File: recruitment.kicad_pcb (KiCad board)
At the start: 2 copper layers, 1 part

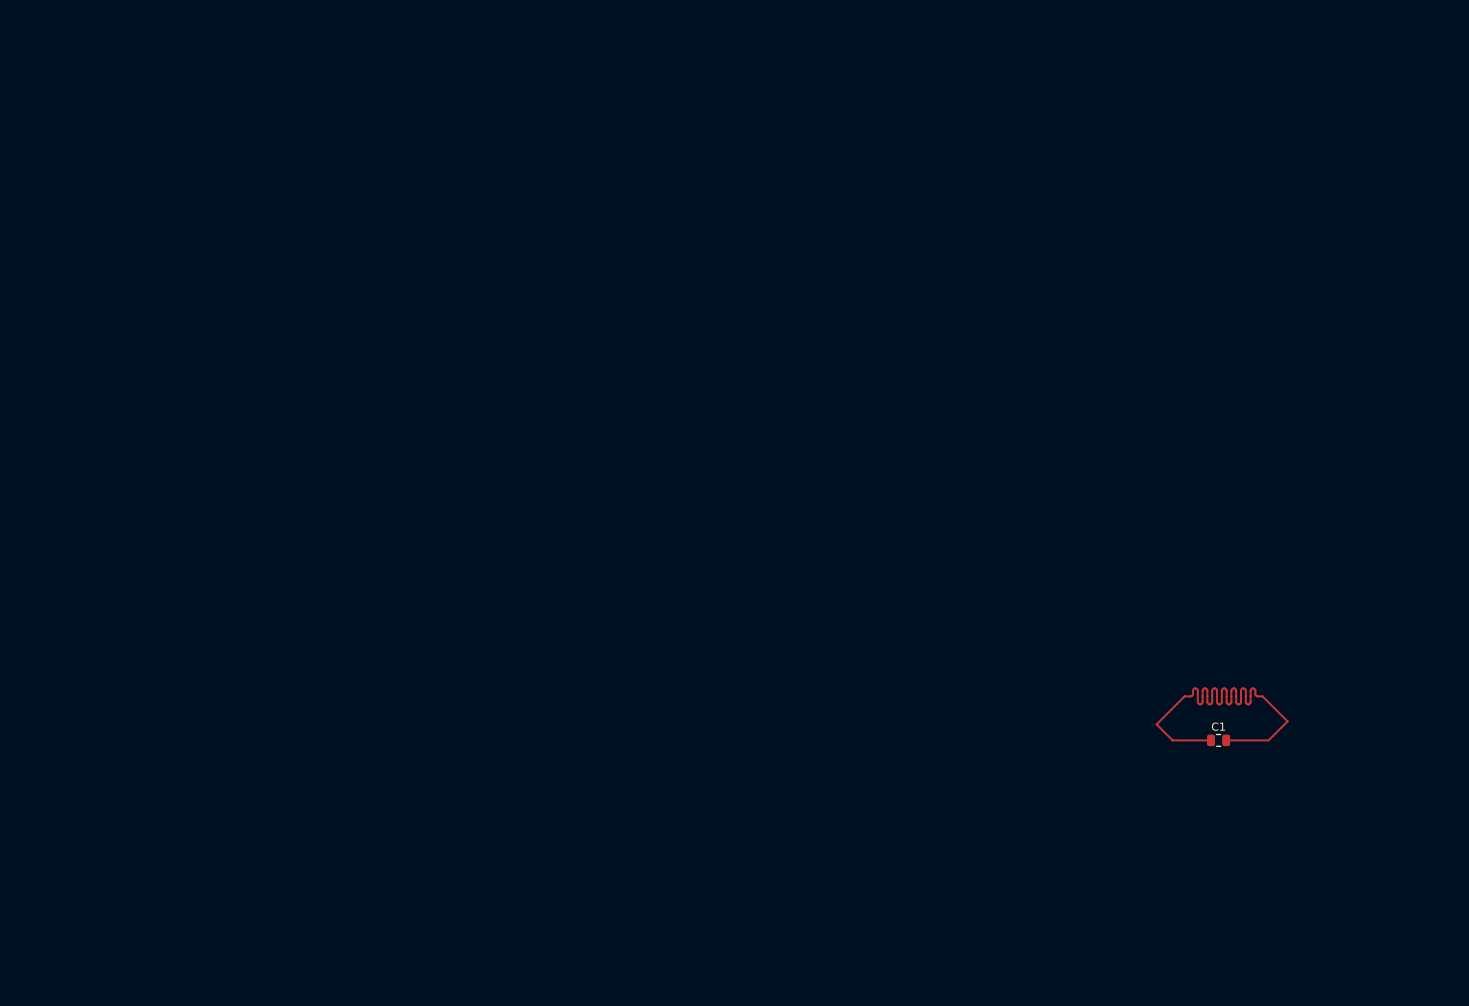
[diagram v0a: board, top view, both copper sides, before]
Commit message: feat: added hall sensor to the monitor system
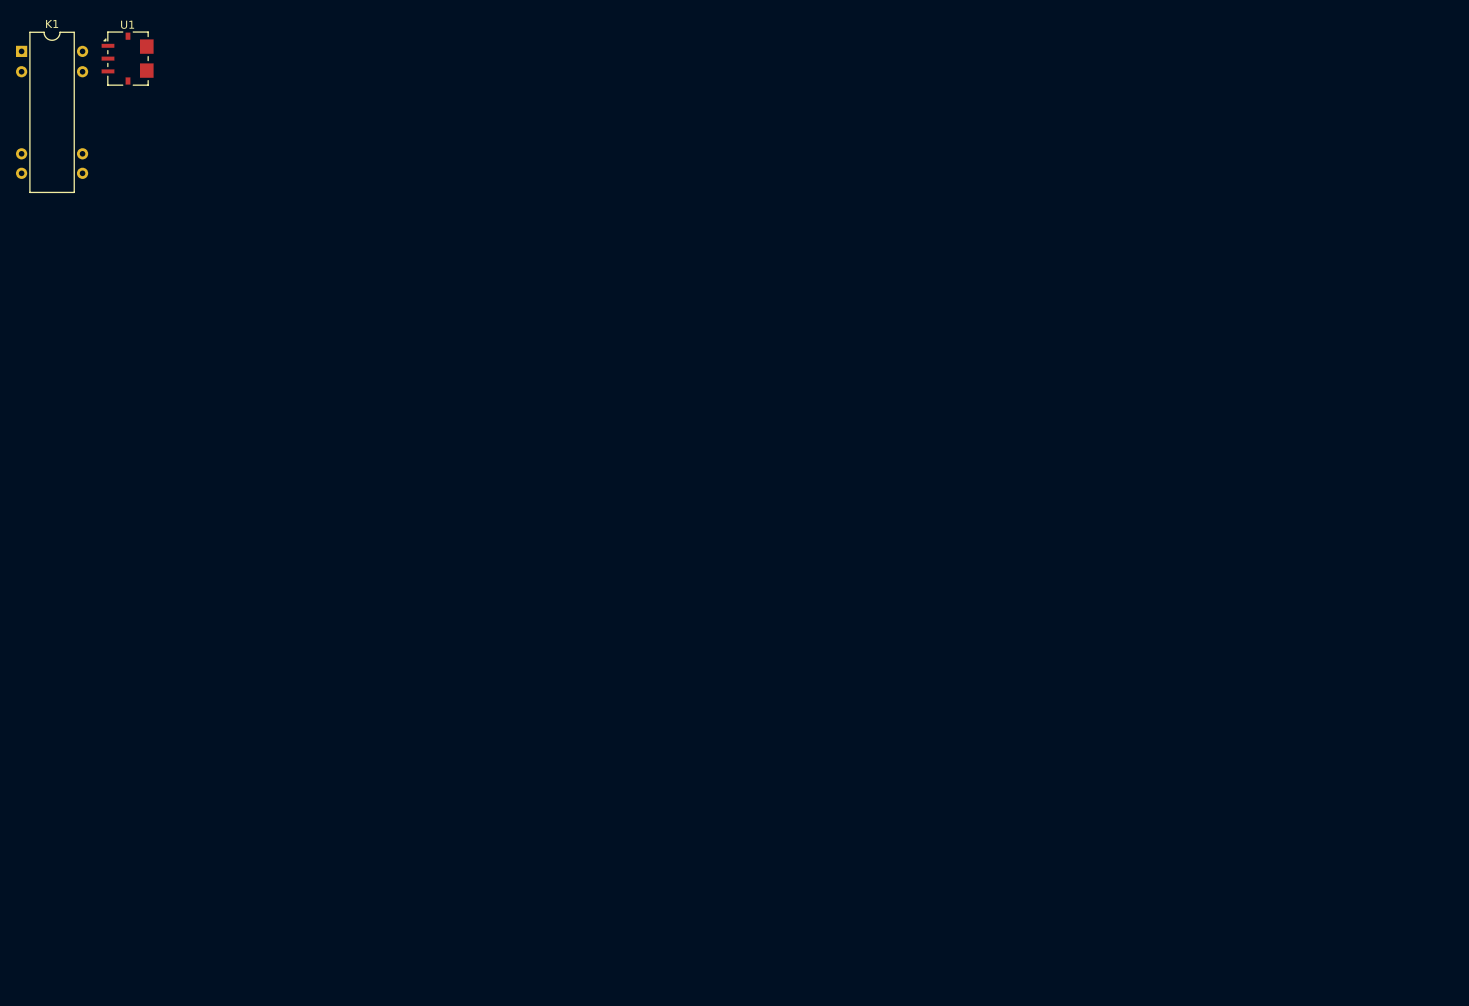
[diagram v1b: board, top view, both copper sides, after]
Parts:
- removed C1: 1F, Capacitor_SMD:C_0805_2012Metric
- added K1: DIPxx-1Axx-11x, Relay_THT:Relay_StandexMeder_DIP_LowProfile, F.Cu at (1.12, 2.62)
- added U1: ACS781xLRTR-050B, Sensor_Current:Allegro_PSOF-7_4.8x6.4mm_P1.60mm, F.Cu at (14.4, 3.52)
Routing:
- net Net-(C1-Pad1): track 57.5 -> 0.00 mm

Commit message: feat + fix on kicad pcb
feat:added mass layer

refactor: moved components for better connection

fix:added missing footprints to resistors etc.

ERC: passed warnings(3)
DRC: errors(42) ;(
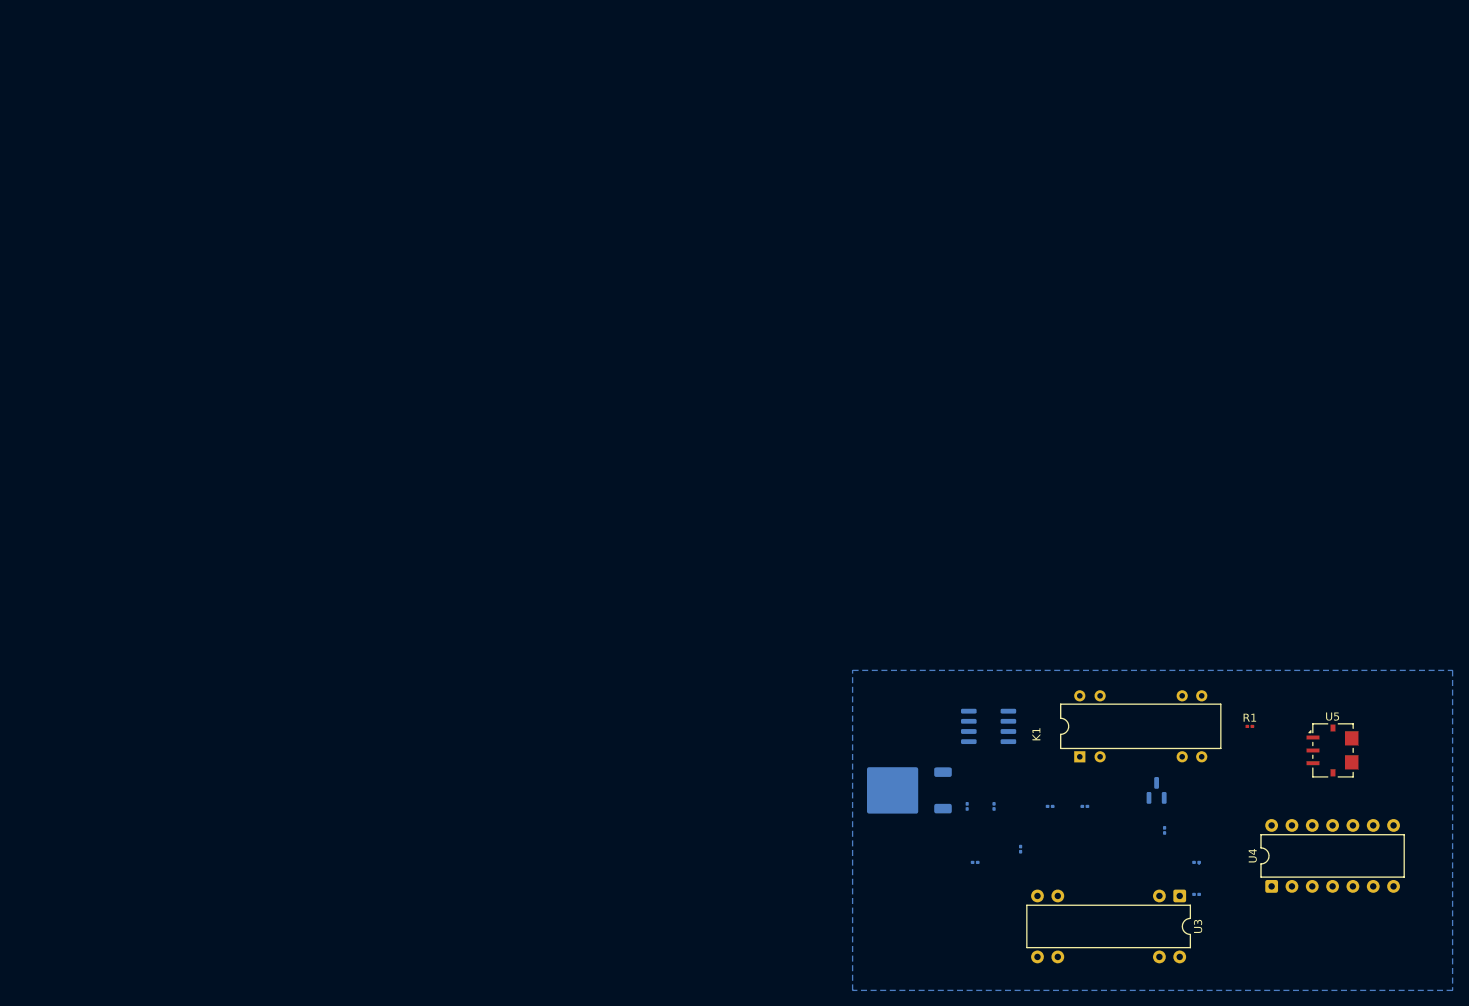
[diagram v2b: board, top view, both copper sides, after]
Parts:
- added C1: 10nF, Capacitor_SMD:C_0201_0603Metric, B.Cu at (119.3, 97.0)
- added C2: 10uF, Capacitor_SMD:C_0201_0603Metric, B.Cu at (122.7, 97.0)
- added Q1: 2N7002, Package_TO_SOT_SMD:SOT-23, B.Cu at (143.0, 95.0)
- added R1: 3,5, Resistor_SMD:R_0201_0603Metric, F.Cu at (154.7, 87.0)
- added R2: 10k, Resistor_SMD:R_0201_0603Metric, B.Cu at (126.0, 102.3)
- added R3: 1, Resistor_SMD:R_0201_0603Metric, B.Cu at (148.0, 108.0)
- added R4: 1,94, Resistor_SMD:R_0201_0603Metric, B.Cu at (129.7, 97.0)
- added R5: 1, Resistor_SMD:R_0201_0603Metric, B.Cu at (134.0, 97.0)
- added R6: 10k, Resistor_SMD:R_0201_0603Metric, B.Cu at (120.3, 104.0)
- added R7: 10k, Resistor_SMD:R_0201_0603Metric, B.Cu at (148.0, 104.0)
- added R8: 10k, Resistor_SMD:R_0201_0603Metric, B.Cu at (144.0, 100.0)
- added U2: L7805, Package_TO_SOT_SMD:TO-252-2, B.Cu at (111.3, 95.0)
- added U3: LM393, Package_DIP:DIP-8-16_W7.62mm, F.Cu at (145.9, 108.2)
- added U4: 7400, Package_DIP:DIP-14_W7.62mm, F.Cu at (157.4, 107.0)
- added U5: ACS780xLRTR-050U, Sensor_Current:Allegro_PSOF-7_4.8x6.4mm_P1.60mm, F.Cu at (165.0, 90.0)
- U1: value ACS781xLRTR-050B -> NE555D; footprint Sensor_Current:Allegro_PSOF-7_4.8x6.4mm_P1.60mm -> Package_SO:SOIC-8_3.9x4.9mm_P1.27mm; moved to B.Cu
- moved K1 159.0 mm to (133.4, 90.8), turned to 90 degrees
- moved U1 136.2 mm to (122.0, 87.0), turned to 180 degrees
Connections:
- net /load_system/LOAD_SUPPLY_IN renamed Net-(U5-IP+)
- K1 pad 2: unconnected-(K1-Pad2) -> GND
- K1 pad 6: unconnected-(K1-Pad6) -> Vcoil
- U1 pad 1: unconnected-(U1-VCC-Pad1) -> GND
- U1 pad 2: unconnected-(U1-GND-Pad2) -> Net-(U1-TR)
- U1 pad 3: unconnected-(U1-VOUT-Pad3) -> VtimerOut
- U1 pad 4: unconnected-(U1-NC-Pad4) -> GND
- U1 pad 5: unconnected-(U1-IP+-Pad5) -> Net-(U1-CV)
- U1 pad 6: unconnected-(U1-IP--Pad6) -> Net-(U1-DIS)
- U1 pad 7: unconnected-(U1-NC-Pad7) -> Net-(U1-DIS)
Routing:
- added copper zone on B.Cu, net GND

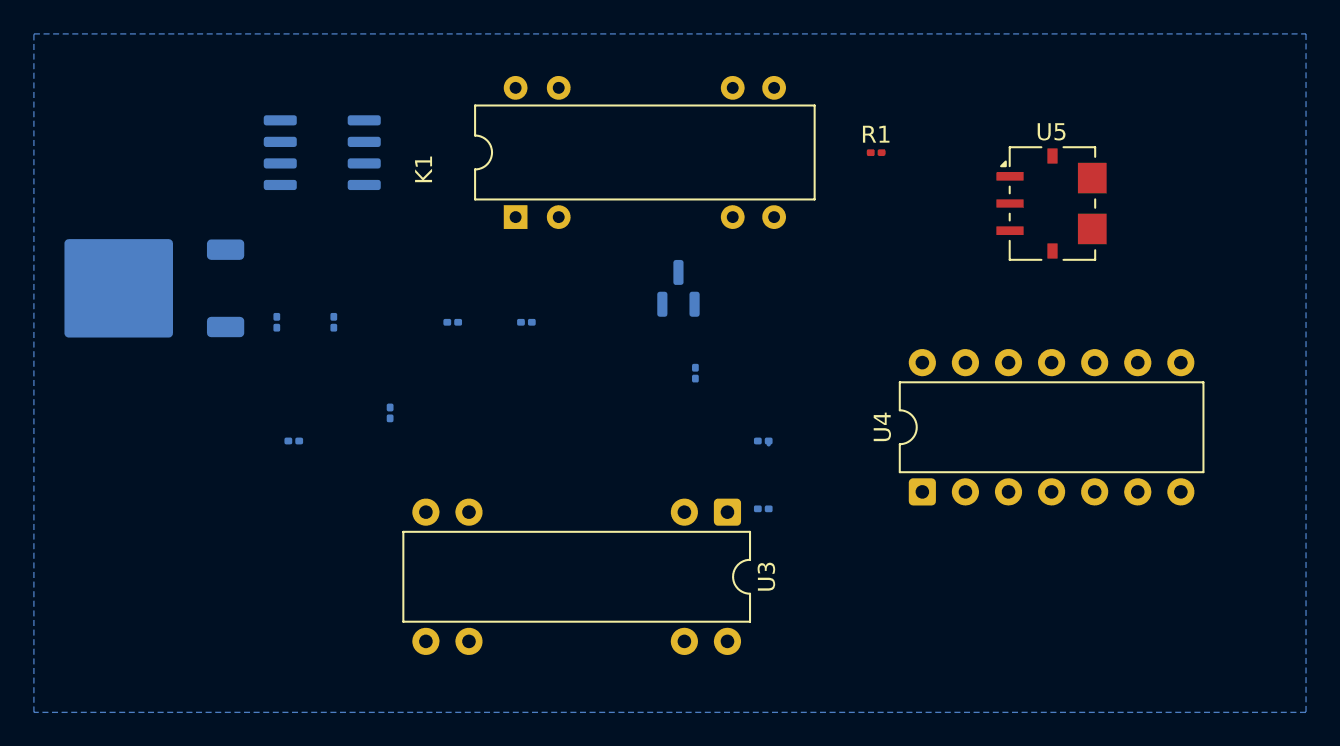
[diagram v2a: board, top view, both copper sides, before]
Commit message: feat + fix + refactor on kicad pcb
feat:added components connections

fix: fixed DRC clearence errors

refactor:moved components in a different layout

ERC: passed warnings(3)
DRC: passed no warnings
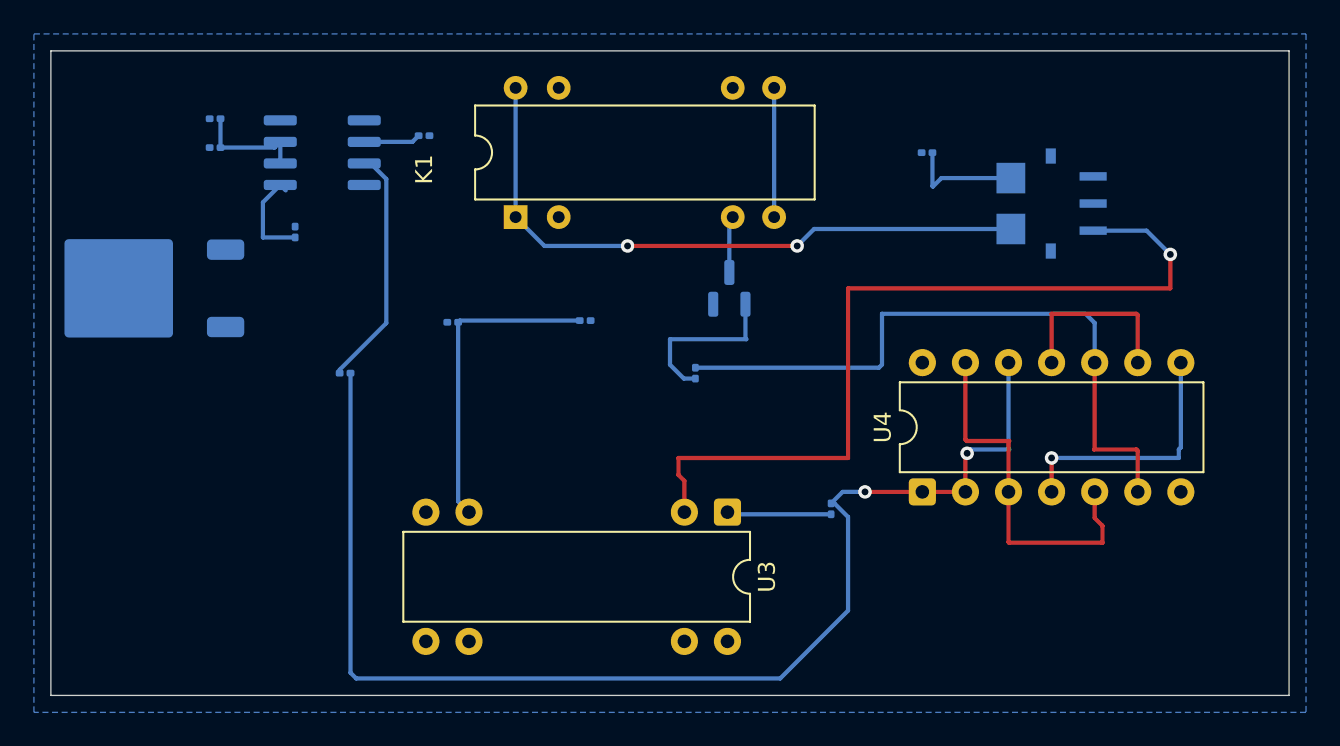
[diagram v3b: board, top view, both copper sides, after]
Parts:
- R1, U5: moved to B.Cu
- moved R3 38.7 mm to (115.7, 86.7), turned to 0 degrees
- moved R2 16.5 mm to (128.0, 86.0), turned to 180 degrees
- moved C2 13.9 mm to (115.7, 85.0), turned to 180 degrees
- moved R7 5.66 mm to (152.0, 108.0), turned to -90 degrees
- moved C1 5.43 mm to (120.4, 91.7)
- moved R6 5.02 mm to (123.3, 100.0)
- moved R5 3.47 mm to (137.5, 96.9)
- moved Q1 3.00 mm to (146.0, 95.0)
- moved R1 3.00 mm to (157.7, 87.0), turned to 180 degrees
- turned U5 to 180 degrees
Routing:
- net Net-(R6-Pad1): track 0.20 -> 73.9 mm, vias 0 -> 2
- net Vout: track 0.00 -> 49.5 mm, vias 0 -> 1
- net Net-(R8-Pad2): track 0.00 -> 39.3 mm
- net Net-(U5-IP+): track 0.00 -> 37.9 mm, vias 0 -> 2
- net Net-(U4-Pad13): track 0.00 -> 21.9 mm
- net Vcompare: track 0.00 -> 18.7 mm
- net Net-(U4-Pad4): track 0.00 -> 15.2 mm, vias 0 -> 1
- net VtimerOut: track 0.00 -> 14.3 mm
- net Net-(U4-Pad11): track 0.00 -> 10.8 mm
- net Net-(Q1-G): track 0.00 -> 9.92 mm
- net /monitor_system/LOAD_SUPPLY_IN: track 0.00 -> 7.62 mm
- net /load_system/LOAD_SUPPLY_IN: track 0.00 -> 6.82 mm
- net Net-(U1-DIS): track 0.00 -> 6.63 mm
- net Net-(R7-Pad2): track 0.00 -> 6.16 mm
- net Net-(U1-CV): track 0.00 -> 5.87 mm
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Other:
- board outline added: 73 x 38 mm
